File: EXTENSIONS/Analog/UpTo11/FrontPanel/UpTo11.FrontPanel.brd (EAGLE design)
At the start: 68 x 58 mm, 3 parts

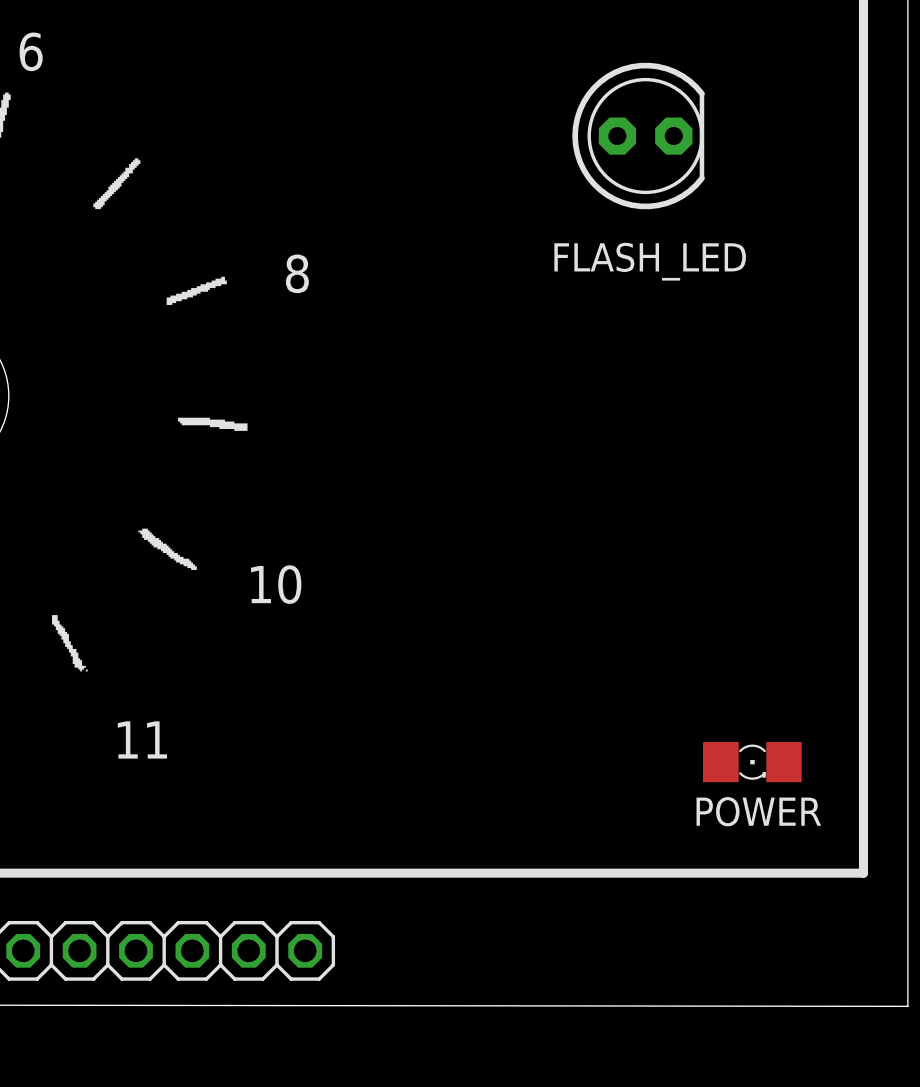
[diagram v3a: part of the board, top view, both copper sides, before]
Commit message: Create UpTo11 Front Panel
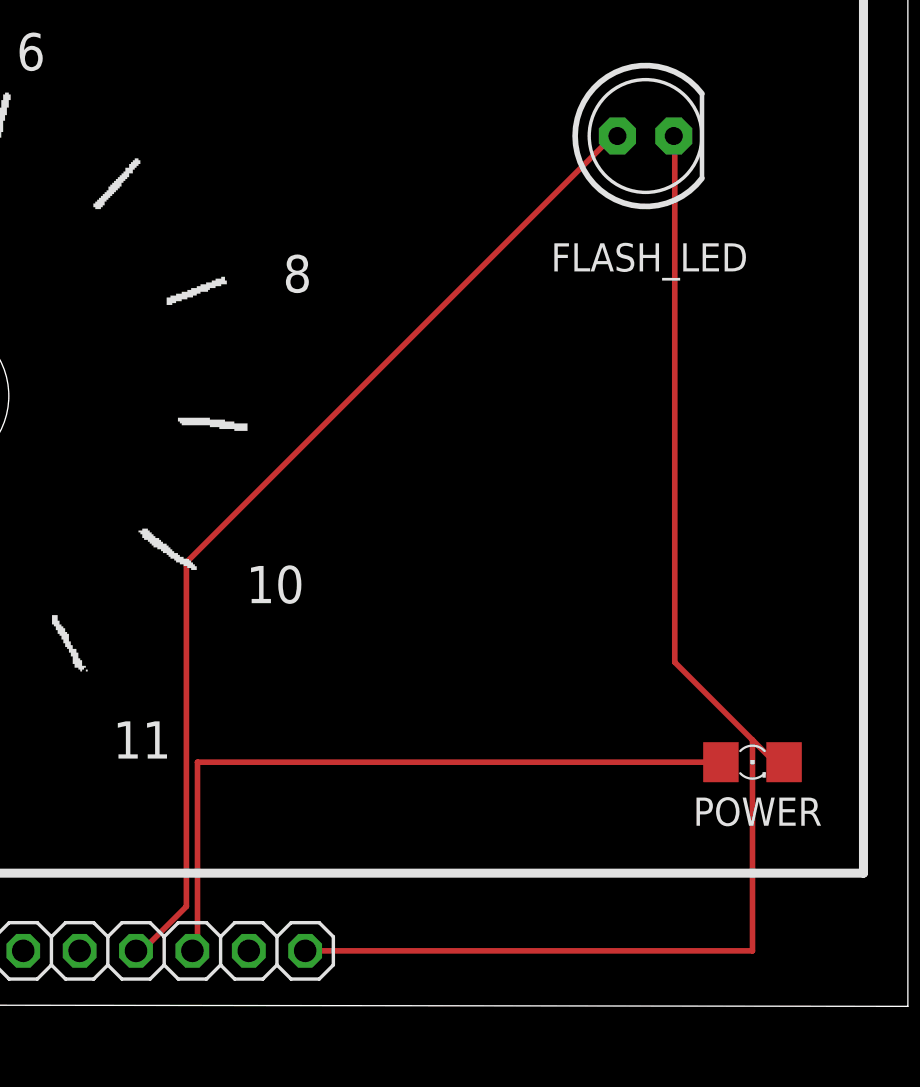
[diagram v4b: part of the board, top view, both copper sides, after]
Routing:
- net GND_EX: track 0.00 -> 60.1 mm
- net LED_FLASH: track 0.00 -> 45.9 mm
- net LED_PWR: track 0.00 -> 32.3 mm
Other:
- board text added: "Up To 11 - Front Panel"
- board text added: "https://bit.ly/2Pm6jPo"
- board text removed: "Up To 11 - MotherBoard"
- board text removed: "https://bit.ly/38Kq3UG"
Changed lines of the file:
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@@
 <layer number="23" name="tOrigins" color="15" fill="1" visible="yes" active="yes"/>
 <layer number="24" name="bOrigins" color="15" fill="1" visible="yes" active="yes"/>
-<layer number="25" name="tNames" color="7" fill="1" visible="no" active="yes"/>
-<layer number="26" name="bNames" color="7" fill="1" visible="yes" active="yes"/>
+<layer number="25" name="tNames" color="7" fill="1" visible="yes" active="yes"/>
+<layer number="26" name="bNames" color="7" fill="1" visible="no" active="yes"/>
 <layer number="27" name="tValues" color="7" fill="1" visible="yes" active="yes"/>
 <layer number="28" name="bValues" color="7" fill="1" visible="yes" active="yes"/>
@@
 <text x="35.5" y="63" size="5.08" layer="25" align="center">Up To 11</text>
 <text x="47.5" y="39" size="2.1844" layer="26" rot="MR0" align="center">MadeInTheUSB.net</text>
-<text x="4.5" y="21" size="1.27" layer="26" rot="MR90" align="center">PCBv1 - 2019.12</text>
-<text x="38" y="66" size="2.1844" layer="26" rot="MR0" align="center">Up To 11 - MotherBoard</text>
+<text x="5.5" y="23" size="1.27" layer="26" rot="MR90" align="center">PCBv1 - 2019.12</text>
+<text x="38" y="66" size="2.1844" layer="26" rot="MR0" align="center">Up To 11 - Front Panel</text>
 <text x="66.5" y="42" size="2.1844" layer="26" rot="MR270" align="center">www.FredericTorres.com</text>
-<text x="38" y="60" size="1.6764" layer="26" rot="MR0" align="center">https://bit.ly/38Kq3UG</text>
+<text x="38" y="60" size="1.6764" layer="26" rot="MR0" align="center">https://bit.ly/2Pm6jPo</text>
 <text x="43.5" y="18.5" size="1.27" layer="26" rot="MR90" align="center">GND</text>
 <text x="41" y="18" size="1.27" layer="26" rot="MR90" align="center">VCC</text>
@@
 <contactref element="FRONT_PANEL_INTERFACE" pad="4"/>
 <contactref element="FLASH_LED" pad="A"/>
-<wire x1="56.91521875" y1="51.206278125" x2="35.23" y2="14.5" width="0" layer="19" extent="1-1"/>
+<wire x1="37.5" y1="16.5" x2="35.5" y2="14.5" width="0.254" layer="1"/>
+<wire x1="37.5" y1="32" x2="37.5" y2="16.5" width="0.254" layer="1"/>
+<wire x1="56.5" y1="51" x2="37.5" y2="32" width="0.254" layer="1"/>
+<wire x1="35.5" y1="14.5" x2="35.23" y2="14.5" width="0.254" layer="1"/>
+<wire x1="56.5" y1="51" x2="56.91521875" y2="51.206278125" width="0.254" layer="1"/>
 </signal>
 <signal name="GND_EX">
@@
 <contactref element="POWER" pad="C"/>
 <contactref element="FLASH_LED" pad="K"/>
-<wire x1="42.85" y1="14.5" x2="64.422" y2="23" width="0" layer="19" extent="1-1"/>
-<wire x1="59.45521875" y1="51.206278125" x2="42.85" y2="14.5" width="0" layer="19" extent="1-1"/>
+<wire x1="59.5" y1="27.5" x2="63" y2="24" width="0.254" layer="1"/>
+<wire x1="63" y1="24" x2="64" y2="23" width="0.254" layer="1"/>
+<wire x1="59.5" y1="51" x2="59.5" y2="27.5" width="0.254" layer="1"/>
+<wire x1="64" y1="23" x2="64.422" y2="23" width="0.254" layer="1"/>
+<wire x1="59.5" y1="51" x2="59.45521875" y2="51.206278125" width="0.254" layer="1"/>
+<wire x1="63" y1="14.5" x2="42.85" y2="14.5" width="0.254" layer="1"/>
+<wire x1="63" y1="24" x2="63" y2="14.5" width="0.254" layer="1"/>
 </signal>
 <signal name="VCC">
@@
 <contactref element="FRONT_PANEL_INTERFACE" pad="3"/>
 <contactref element="POWER" pad="A"/>
-<wire x1="61.578" y1="23" x2="37.77" y2="14.5" width="0" layer="19" extent="1-1"/>
+<wire x1="38" y1="23" x2="61.578" y2="23" width="0.254" layer="1"/>
+<wire x1="38" y1="14.5" x2="38" y2="23" width="0.254" layer="1"/>
+<wire x1="38" y1="14.5" x2="37.77" y2="14.5" width="0.254" layer="1"/>
 </signal>
 <signal name="POT_IN">

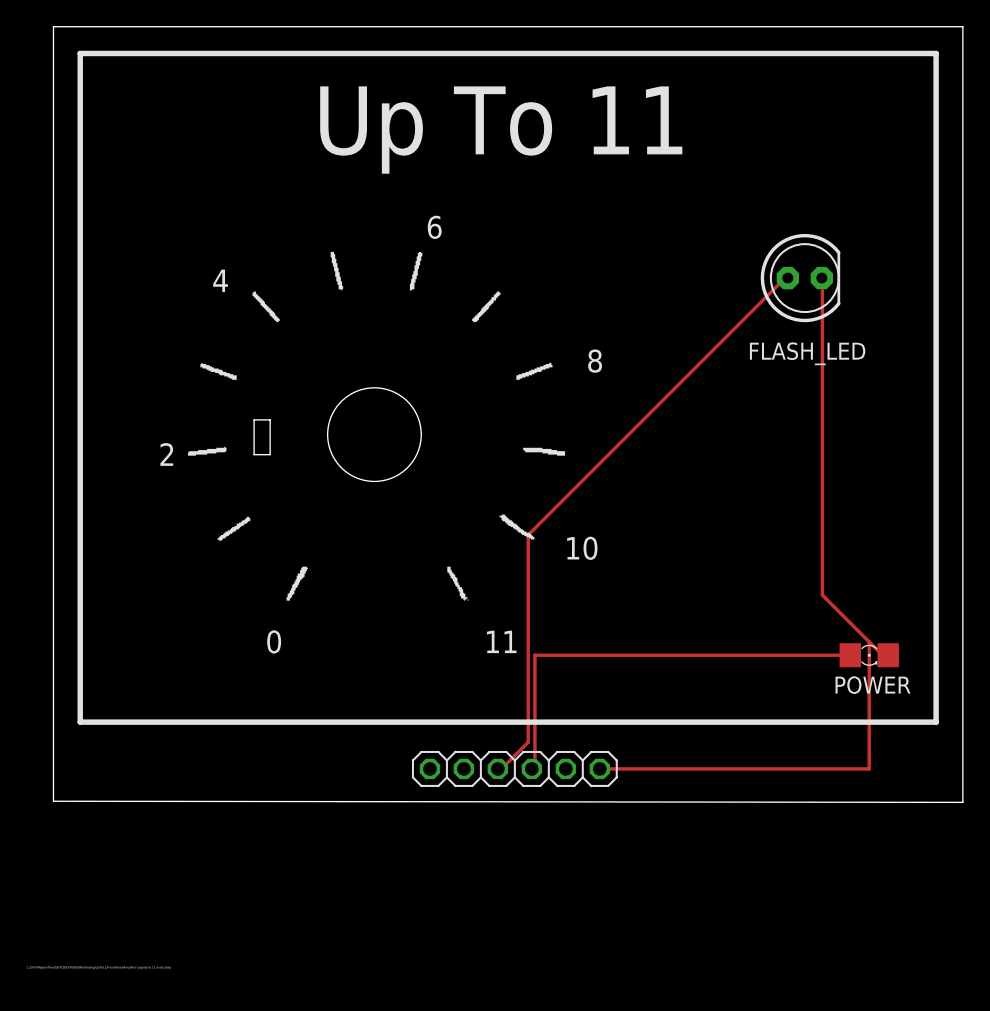
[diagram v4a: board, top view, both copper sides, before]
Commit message: Create UpTo11 Front Panel
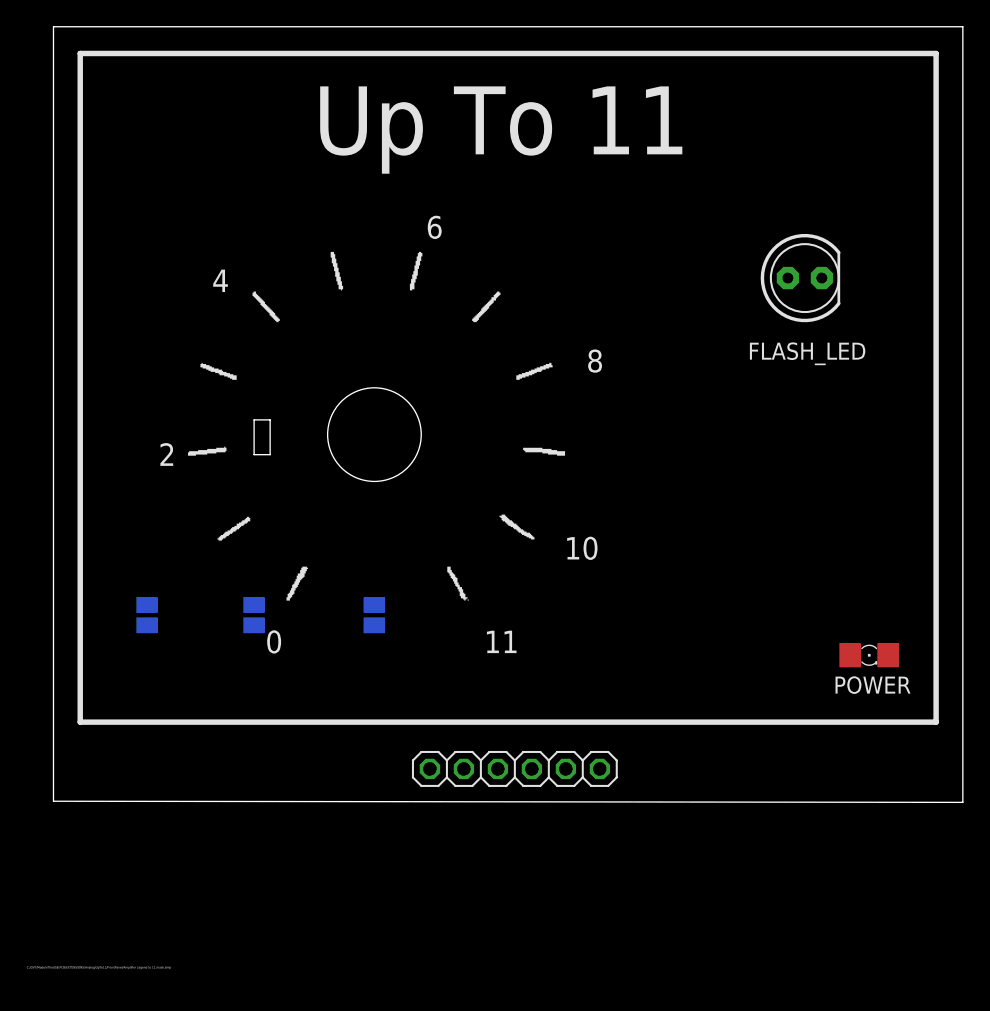
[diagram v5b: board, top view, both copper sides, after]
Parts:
- added POT_GND_(RIGHT), POT_IN_(MIDDLE), POT_OUT_(LEFT): (no value), microbuilder:SOLDERJUMPER_REFLOW
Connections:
- net GND_EX: now also POT_GND_(RIGHT).2
- net POT_IN: now also POT_IN_(MIDDLE).2
- net POT_OUT: now also POT_OUT_(LEFT).2
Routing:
- net GND_EX: track 60.1 -> 0.00 mm
- net LED_FLASH: track 45.9 -> 0.00 mm
- net LED_PWR: track 32.3 -> 0.00 mm
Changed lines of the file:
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@@
 <layer number="23" name="tOrigins" color="15" fill="1" visible="yes" active="yes"/>
 <layer number="24" name="bOrigins" color="15" fill="1" visible="yes" active="yes"/>
-<layer number="25" name="tNames" color="7" fill="1" visible="yes" active="yes"/>
-<layer number="26" name="bNames" color="7" fill="1" visible="no" active="yes"/>
+<layer number="25" name="tNames" color="7" fill="1" visible="no" active="yes"/>
+<layer number="26" name="bNames" color="7" fill="1" visible="yes" active="yes"/>
 <layer number="27" name="tValues" color="7" fill="1" visible="yes" active="yes"/>
 <layer number="28" name="bValues" color="7" fill="1" visible="yes" active="yes"/>
@@
 <text x="35.5" y="63" size="5.08" layer="25" align="center">Up To 11</text>
 <text x="47.5" y="39" size="2.1844" layer="26" rot="MR0" align="center">MadeInTheUSB.net</text>
-<text x="5.5" y="23" size="1.27" layer="26" rot="MR90" align="center">PCBv1 - 2019.12</text>
+<text x="6.5" y="55" size="1.27" layer="26" rot="MR90" align="center">PCBv1 - 2019.12</text>
 <text x="38" y="66" size="2.1844" layer="26" rot="MR0" align="center">Up To 11 - Front Panel</text>
 <text x="66.5" y="42" size="2.1844" layer="26" rot="MR270" align="center">www.FredericTorres.com</text>
@@
 <attribute name="VALUE" x="61.38561875" y="49.402878125" size="1.27" layer="27" ratio="10"/>
 </element>
+<element name="POT_GND_(RIGHT)" library="microbuilder" package="SOLDERJUMPER_REFLOW" value="" x="9" y="26" smashed="yes" rot="MR270">
+<attribute name="NAME" x="6.73" y="26.651" size="1.27" layer="26" ratio="18" rot="MR270" align="center"/>
+<attribute name="VALUE" x="9" y="25.5999" size="0.02" layer="28" rot="MR270"/>
+</element>
+<element name="POT_IN_(MIDDLE)" library="microbuilder" package="SOLDERJUMPER_REFLOW" value="" x="17" y="26" smashed="yes" rot="MR270">
+<attribute name="NAME" x="14.73" y="26.651" size="1.27" layer="26" ratio="18" rot="MR270" align="center"/>
+<attribute name="VALUE" x="17" y="25.5999" size="0.02" layer="28" rot="MR270"/>
+</element>
+<element name="POT_OUT_(LEFT)" library="microbuilder" package="SOLDERJUMPER_REFLOW" value="" x="26" y="26" smashed="yes" rot="MR270">
+<attribute name="NAME" x="22.73" y="26.651" size="1.27" layer="26" ratio="18" rot="MR270" align="center"/>
+<attribute name="VALUE" x="26" y="25.5999" size="0.02" layer="28" rot="MR270"/>
+</element>
 </elements>
 <signals>
@@
 <contactref element="FRONT_PANEL_INTERFACE" pad="4"/>
 <contactref element="FLASH_LED" pad="A"/>
-<wire x1="37.5" y1="16.5" x2="35.5" y2="14.5" width="0.254" layer="1"/>
-<wire x1="37.5" y1="32" x2="37.5" y2="16.5" width="0.254" layer="1"/>
-<wire x1="56.5" y1="51" x2="37.5" y2="32" width="0.254" layer="1"/>
-<wire x1="35.5" y1="14.5" x2="35.23" y2="14.5" width="0.254" layer="1"/>
-<wire x1="56.5" y1="51" x2="56.91521875" y2="51.206278125" width="0.254" layer="1"/>
+<wire x1="56.91521875" y1="51.206278125" x2="35.23" y2="14.5" width="0" layer="19" extent="1-1"/>
 </signal>
 <signal name="GND_EX">
@@
 <contactref element="POWER" pad="C"/>
 <contactref element="FLASH_LED" pad="K"/>
-<wire x1="59.5" y1="27.5" x2="63" y2="24" width="0.254" layer="1"/>
-<wire x1="63" y1="24" x2="64" y2="23" width="0.254" layer="1"/>
-<wire x1="59.5" y1="51" x2="59.5" y2="27.5" width="0.254" layer="1"/>
-<wire x1="64" y1="23" x2="64.422" y2="23" width="0.254" layer="1"/>
-<wire x1="59.5" y1="51" x2="59.45521875" y2="51.206278125" width="0.254" layer="1"/>
-<wire x1="63" y1="14.5" x2="42.85" y2="14.5" width="0.254" layer="1"/>
-<wire x1="63" y1="24" x2="63" y2="14.5" width="0.254" layer="1"/>
+<contactref element="POT_GND_(RIGHT)" pad="2"/>
+<wire x1="64.422" y1="23" x2="59.45521875" y2="51.206278125" width="0" layer="19" extent="1-1"/>
+<wire x1="42.85" y1="14.5" x2="64.422" y2="23" width="0" layer="19" extent="1-1"/>
+<wire x1="9" y1="25.238" x2="42.85" y2="14.5" width="0" layer="19" extent="1-1"/>
 </signal>
 <signal name="VCC">
@@
 <contactref element="FRONT_PANEL_INTERFACE" pad="3"/>
 <contactref element="POWER" pad="A"/>
-<wire x1="38" y1="23" x2="61.578" y2="23" width="0.254" layer="1"/>
-<wire x1="38" y1="14.5" x2="38" y2="23" width="0.254" layer="1"/>
-<wire x1="38" y1="14.5" x2="37.77" y2="14.5" width="0.254" layer="1"/>
+<wire x1="61.578" y1="23" x2="37.77" y2="14.5" width="0" layer="19" extent="1-1"/>
 </signal>
 <signal name="POT_IN">
 <contactref element="FRONT_PANEL_INTERFACE" pad="5"/>
+<contactref element="POT_IN_(MIDDLE)" pad="2"/>
+<wire x1="17" y1="25.238" x2="32.69" y2="14.5" width="0" layer="19" extent="1-1"/>
 </signal>
 <signal name="POT_OUT">
 <contactref element="FRONT_PANEL_INTERFACE" pad="6"/>
+<contactref element="POT_OUT_(LEFT)" pad="2"/>
+<wire x1="26" y1="25.238" x2="30.15" y2="14.5" width="0" layer="19" extent="1-1"/>
 </signal>
 </signals>
